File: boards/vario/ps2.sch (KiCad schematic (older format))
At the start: 57 parts, among them Q1 Q_NMOS_DSG, Q2 Q_NMOS_DSG, Q3 Q_PMOS_DGS, U10 74LS161, U11 74HC244, U12 74HC74, U13 74HC74, U14 74LS08, U15 74HC74, U16 74HC74, U17 74LS161, U18 74HC273, U19 74LS280, U20 74LS151, U21 74LS151, U22 74HC244, U23 74LS280, U24 74LS10, U25 74LS08, U26 74LS04, U27 74LS32, U28 74LS32, U29 74LS32, U30 74LS32, U7 74HC14, U8 74HC273, U9 74HC273

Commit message: SPI: implement missing logic
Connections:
- net recv_clk: no longer U7.3
- net clk_in: no longer names the net of U7.4
- no-connect marks 13 -> 17
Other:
- moved on the sheet: U7B
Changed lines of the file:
@@
 Text HLabel 1100 2800 0    50   Input ~ 0
 a
-Text GLabel 1100 1150 0    50   Input ~ 0
+Text GLabel 1100 1150 0    50   Output ~ 0
 ~rst
 Text Label 1100 1150 0    50   ~ 0
@@
 L 74xx:74HC14 U7
 U 2 1 5FE912BF
-P 12200 2000
-F 0 "U7" H 12200 1683 50  0000 C CNN
-F 1 "74HC14" H 12200 1774 50  0000 C CNN
-F 2 "" H 12200 2000 50  0001 C CNN
-F 3 "http://www.ti.com/lit/gpn/sn74HC14" H 12200 2000 50  0001 C CNN
-	2    12200 2000
+P 15250 4600
+F 0 "U7" H 15250 4283 50  0000 C CNN
+F 1 "74HC14" H 15250 4374 50  0000 C CNN
+F 2 "" H 15250 4600 50  0001 C CNN
+F 3 "http://www.ti.com/lit/gpn/sn74HC14" H 15250 4600 50  0001 C CNN
+	2    15250 4600
 	-1   0    0    1
 $EndComp
@@
 Wire Wire Line
 	12500 2000 12850 2000
-Text Label 11900 2000 2    50   ~ 0
-clk_in
 Wire Wire Line
 	12500 3150 12850 3150
@@
 Text Label 9400 5550 0    50   ~ 0
 ~recv_rdy
-Text GLabel 1100 1400 0    50   Input ~ 0
+Text GLabel 1100 1400 0    50   3State ~ 0
 ~rdy
 Text Label 1100 1400 0    50   ~ 0
@@
 	1    0    0    -1
 $EndComp
+NoConn ~ 2650 12700
+NoConn ~ 7550 10950
+NoConn ~ 11050 8600
+NoConn ~ 6500 12750
 Wire Bus Line
 	1550 2200 1550 3200

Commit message: PS/2: different select signals
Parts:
- removed C25: 0.1, symbol Device:C
- removed Q1, Q2: Q_NMOS_DSG, symbol Device:Q_NMOS_DSG
- removed Q3: Q_PMOS_DGS, symbol Device:Q_PMOS_DGS
- removed U27: 74LS32, symbol 74xx:74LS32
- added Q? (x3): Q_NMOS_GSD, symbol Device:Q_NMOS_GSD
- added U33: 74LS08, symbol 74xx:74LS08
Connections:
- net a is gone; now on net ~data_out: U26.3
- net GND: now also Q?.2 (S), Q?.2 (S), Q?.2 (S)
- net VCC: now also U7.13; no longer U30.12, U30.13
- net data_in: now also U7.4; no longer U7.10
- net data_out: now also U26.4; no longer U26.12
- net ps2_clk: now also U7.11, Q?.3 (D); no longer U7.1
- net ps2_data: now also U7.1, Q?.3 (D); no longer U7.13
- net rdy: now also U26.13, Q?.3 (D)
- net recv_clk: now also U7.10; no longer U7.2
- net ~clk_out: now also Q?.1 (G)
- net ~data_in: now also U7.2, U7.3; no longer U7.11, U7.12
- net ~data_oe: now also U30.11
- net ~data_out: now also Q?.1 (G); no longer U26.13
- net ~data_sel: now also U30.12, U33.4
- net ~oe: now also U30.13
- net ~rdy: now also U26.12, Q?.1 (G)
- net ~sel: now also U33.6
- net ~status_sel: now also U30.10, U33.5
- net ~status_we: now also U30.8
- net ~we: now also U30.9
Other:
- moved on the sheet: U26B, U26F, U30C, U30D, U7A, U7B, U7E, U7F

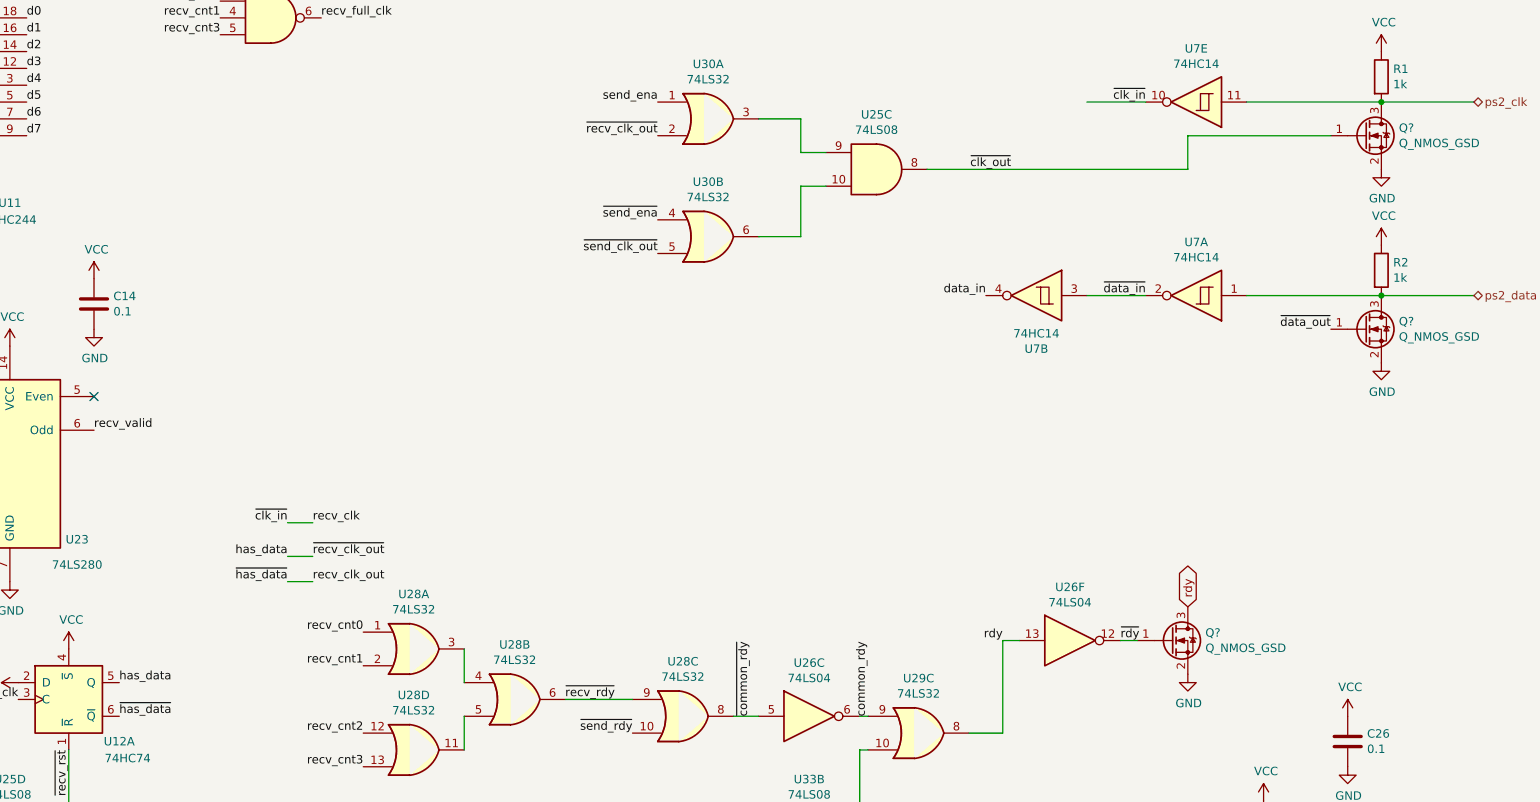
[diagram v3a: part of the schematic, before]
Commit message: Vario: status LEDs
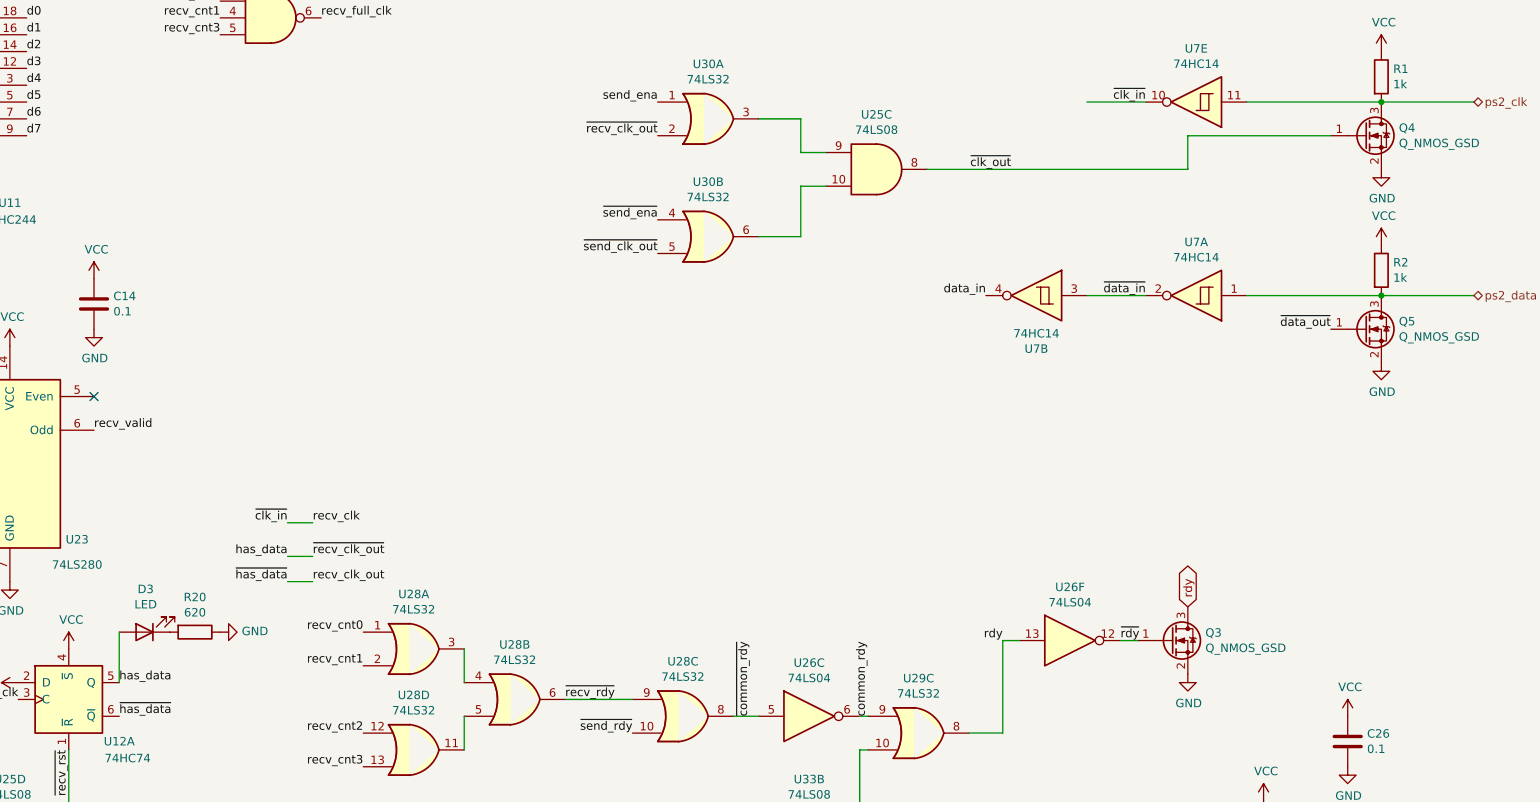
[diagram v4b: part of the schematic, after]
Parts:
- added D3: LED, symbol Device:LED
- added R20: 620, symbol Device:R
- gave numbers to parts that had none: 3
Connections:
- net GND: now also R20.1
- net has_data: now also D3.2 (A)
- new net: D3.1 (K), R20.2
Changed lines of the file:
@@
 $EndComp
 $Comp
-L Device:Q_NMOS_GSD Q?
+L Device:Q_NMOS_GSD Q4
 U 1 1 60239241
 P 14150 2200
-F 0 "Q?" H 14354 2246 50  0000 L CNN
+F 0 "Q4" H 14354 2246 50  0000 L CNN
 F 1 "Q_NMOS_GSD" H 14354 2155 50  0000 L CNN
 F 2 "" H 14350 2300 50  0001 C CNN
@@
 $EndComp
 $Comp
-L Device:Q_NMOS_GSD Q?
+L Device:Q_NMOS_GSD Q5
 U 1 1 6023C476
 P 14150 3350
-F 0 "Q?" H 14354 3396 50  0000 L CNN
+F 0 "Q5" H 14354 3396 50  0000 L CNN
 F 1 "Q_NMOS_GSD" H 14354 3305 50  0000 L CNN
 F 2 "" H 14350 3450 50  0001 C CNN
@@
 $EndComp
 $Comp
-L Device:Q_NMOS_GSD Q?
+L Device:Q_NMOS_GSD Q3
 U 1 1 6023F5E2
 P 13000 5200
-F 0 "Q?" H 13204 5246 50  0000 L CNN
+F 0 "Q3" H 13204 5246 50  0000 L CNN
 F 1 "Q_NMOS_GSD" H 13204 5155 50  0000 L CNN
 F 2 "" H 13200 5300 50  0001 C CNN
@@
 $EndComp
 $Comp
-L power:GND #PWR?
+L power:GND #PWR0227
 U 1 1 6023FF8E
 P 13100 5400
-F 0 "#PWR?" H 13100 5150 50  0001 C CNN
+F 0 "#PWR0227" H 13100 5150 50  0001 C CNN
 F 1 "GND" H 13105 5227 50  0000 C CNN
 F 2 "" H 13100 5400 50  0001 C CNN
@@
 Wire Wire Line
 	11150 5850 11200 5850
+$Comp
+L Device:LED D?
+U 1 1 6039F9A4
+P 6900 5150
+AR Path="/5FE5ABE2/6039F9A4" Ref="D?"  Part="1"
+AR Path="/5FE853A4/6039F9A4" Ref="D3"  Part="1"
+F 0 "D3" H 6893 4895 50  0000 C CNN
+F 1 "LED" H 6893 4986 50  0000 C CNN
+F 2 "" H 6900 5150 50  0001 C CNN
+F 3 "~" H 6900 5150 50  0001 C CNN
+	1    6900 5150
+	-1   0    0    1
+$EndComp
+$Comp
+L Device:R R?
+U 1 1 6039F9AB
+P 7200 5150
+AR Path="/5FE5ABE2/6039F9AB" Ref="R?"  Part="1"
+AR Path="/5FE853A4/6039F9AB" Ref="R20"  Part="1"
+F 0 "R20" V 6993 5150 50  0000 C CNN
+F 1 "620" V 7084 5150 50  0000 C CNN
+F 2 "" V 7130 5150 50  0001 C CNN
+F 3 "~" H 7200 5150 50  0001 C CNN
+	1    7200 5150
+	0    1    1    0
+$EndComp
+$Comp
+L power:GND #PWR?
+U 1 1 6039F9B1
+P 7350 5150
+AR Path="/6039F9B1" Ref="#PWR?"  Part="1"
+AR Path="/5FE5ABE2/6039F9B1" Ref="#PWR?"  Part="1"
+AR Path="/5FE853A4/6039F9B1" Ref="#PWR0226"  Part="1"
+F 0 "#PWR0226" H 7350 4900 50  0001 C CNN
+F 1 "GND" V 7355 5022 50  0000 R CNN
+F 2 "" H 7350 5150 50  0001 C CNN
+F 3 "" H 7350 5150 50  0001 C CNN
+	1    7350 5150
+	0    -1   -1   0
+$EndComp
+Wire Wire Line
+	6750 5450 6750 5150
 Wire Bus Line
 	1550 2200 1550 3200

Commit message: Vario: component names and footprints
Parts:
- C1, C10, C11, C12, C13, C14, C15, C16, C17, C18, C19, C2, C20, C21, C22, C23, C24, C26, C3, C4, C5, C6, C7, C8, C9: footprint (none) -> Capacitor_SMD:C_0805_2012Metric
- D3: footprint (none) -> LED_SMD:LED_0805_2012Metric
- Q3, Q4, Q5: footprint (none) -> Package_TO_SOT_SMD:SOT-23
- R1, R2, R20, R3, R4: footprint (none) -> Resistor_SMD:R_0805_2012Metric
- U10, U17: value 74LS161 -> 74HC161PW; footprint (none) -> Package_SO:TSSOP-16_4.4x5mm_P0.65mm
- U11, U22: value 74HC244 -> MC74HC244ADT; footprint (none) -> Package_SO:TSSOP-20_4.4x6.5mm_P0.65mm
- U12, U13, U15, U16: value 74HC74 -> 74HC74PW; footprint (none) -> Package_SO:TSSOP-14_4.4x5mm_P0.65mm
- U14, U25, U33: value 74LS08 -> 74HC08PW; footprint (none) -> Package_SO:TSSOP-14_4.4x5mm_P0.65mm
- U18, U8, U9: value 74HC273 -> 74HC273PW; footprint (none) -> Package_SO:TSSOP-20_4.4x6.5mm_P0.65mm
- U19, U23: value 74LS280 -> CD74HC280MT; footprint (none) -> Package_SO:SOIC-14_3.9x8.7mm_P1.27mm
- U20, U21: value 74LS151 -> MC74HC151ADTR2G; footprint (none) -> Package_SO:TSSOP-16_4.4x5mm_P0.65mm
- U24: value 74LS10 -> SN74LV10APW; footprint (none) -> Package_SO:TSSOP-14_4.4x5mm_P0.65mm
- U26: value 74LS04 -> 74HC04PW; footprint (none) -> Package_SO:TSSOP-14_4.4x5mm_P0.65mm
- U28, U29, U30: value 74LS32 -> SN74HC32PWR; footprint (none) -> Package_SO:TSSOP-14_4.4x5mm_P0.65mm
- U7: value 74HC14 -> SN74LV14APW; footprint (none) -> Package_SO:TSSOP-14_4.4x5mm_P0.65mm

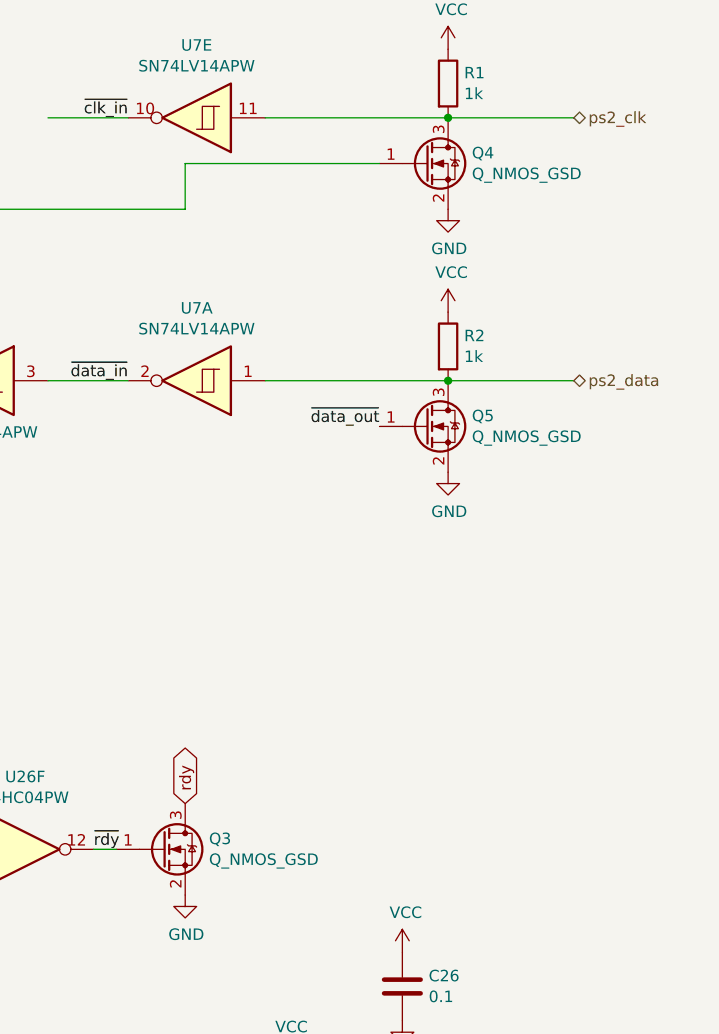
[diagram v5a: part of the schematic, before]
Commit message: Vario: transistors and capacitors
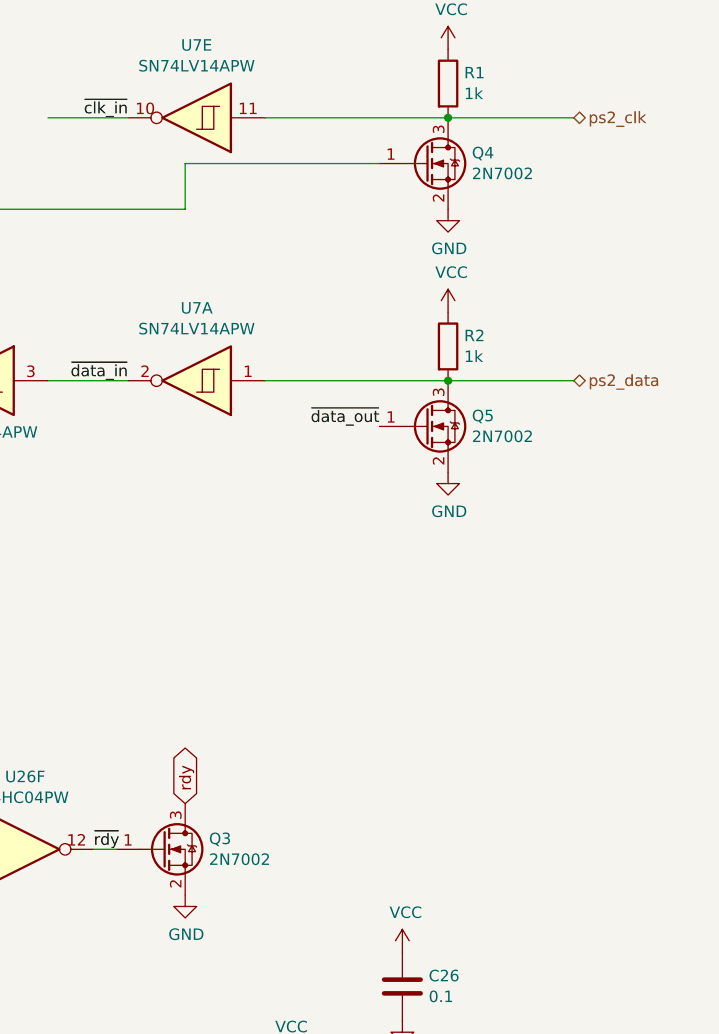
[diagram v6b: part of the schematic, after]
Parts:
- Q3, Q4, Q5: value Q_NMOS_GSD -> 2N7002
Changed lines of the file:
@@
 P 14150 2200
 F 0 "Q4" H 14354 2246 50  0000 L CNN
-F 1 "Q_NMOS_GSD" H 14354 2155 50  0000 L CNN
+F 1 "2N7002" H 14354 2155 50  0000 L CNN
 F 2 "Package_TO_SOT_SMD:SOT-23" H 14350 2300 50  0001 C CNN
 F 3 "~" H 14150 2200 50  0001 C CNN
@@
 P 14150 3350
 F 0 "Q5" H 14354 3396 50  0000 L CNN
-F 1 "Q_NMOS_GSD" H 14354 3305 50  0000 L CNN
+F 1 "2N7002" H 14354 3305 50  0000 L CNN
 F 2 "Package_TO_SOT_SMD:SOT-23" H 14350 3450 50  0001 C CNN
 F 3 "~" H 14150 3350 50  0001 C CNN
@@
 P 13000 5200
 F 0 "Q3" H 13204 5246 50  0000 L CNN
-F 1 "Q_NMOS_GSD" H 13204 5155 50  0000 L CNN
+F 1 "2N7002" H 13204 5155 50  0000 L CNN
 F 2 "Package_TO_SOT_SMD:SOT-23" H 13200 5300 50  0001 C CNN
 F 3 "~" H 13000 5200 50  0001 C CNN
